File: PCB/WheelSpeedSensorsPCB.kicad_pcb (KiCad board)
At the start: 2 copper layers, 60 x 90 mm, 21 parts, among them J1 RearLeftWheel, J10 FrontRightShock, J11 RearRightShock, J2 FrontRightWheel, J3 RearRightWheel, J4 Conn_01x02_Pin, J5 FrontLeftWheel, J6 RearLeftShock, J7 VehicleBus, J8 Conn_01x02_Pin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

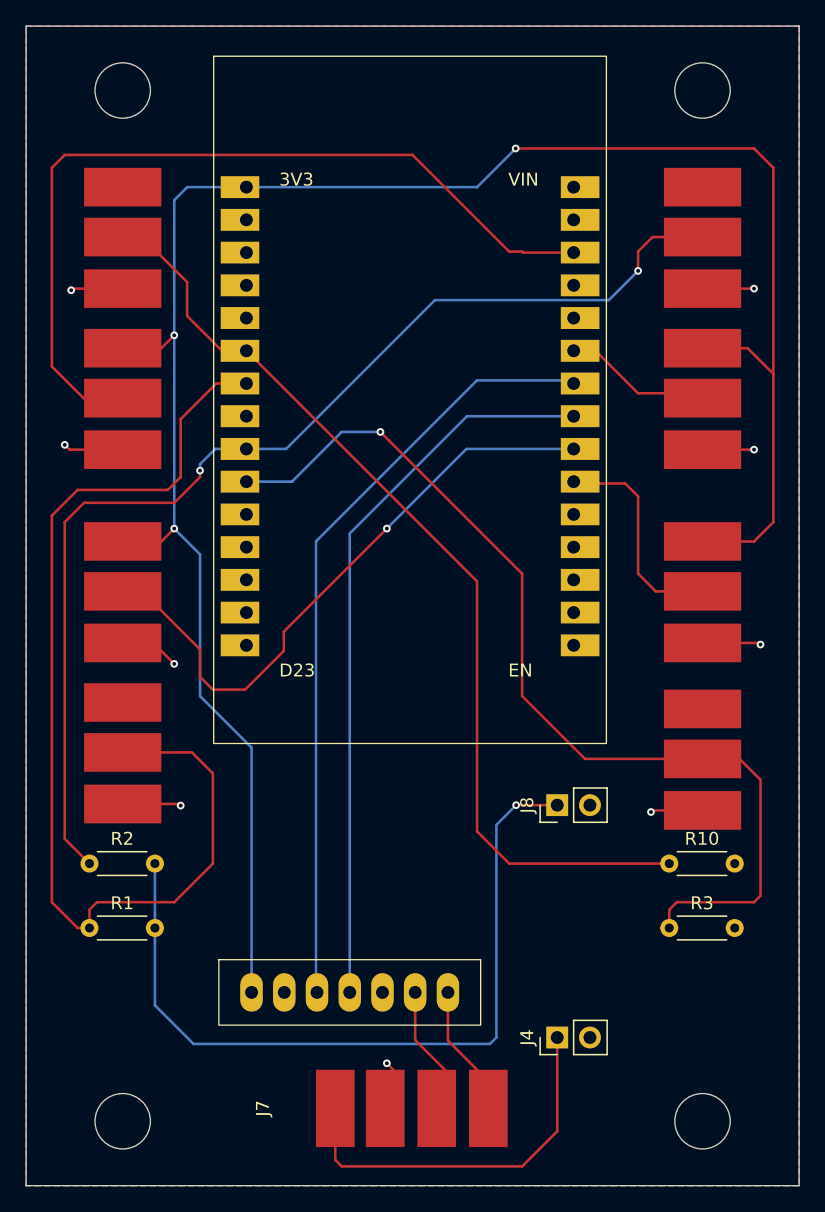
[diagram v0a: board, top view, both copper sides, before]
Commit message: Update PCB and GBRs to have Silkscreen
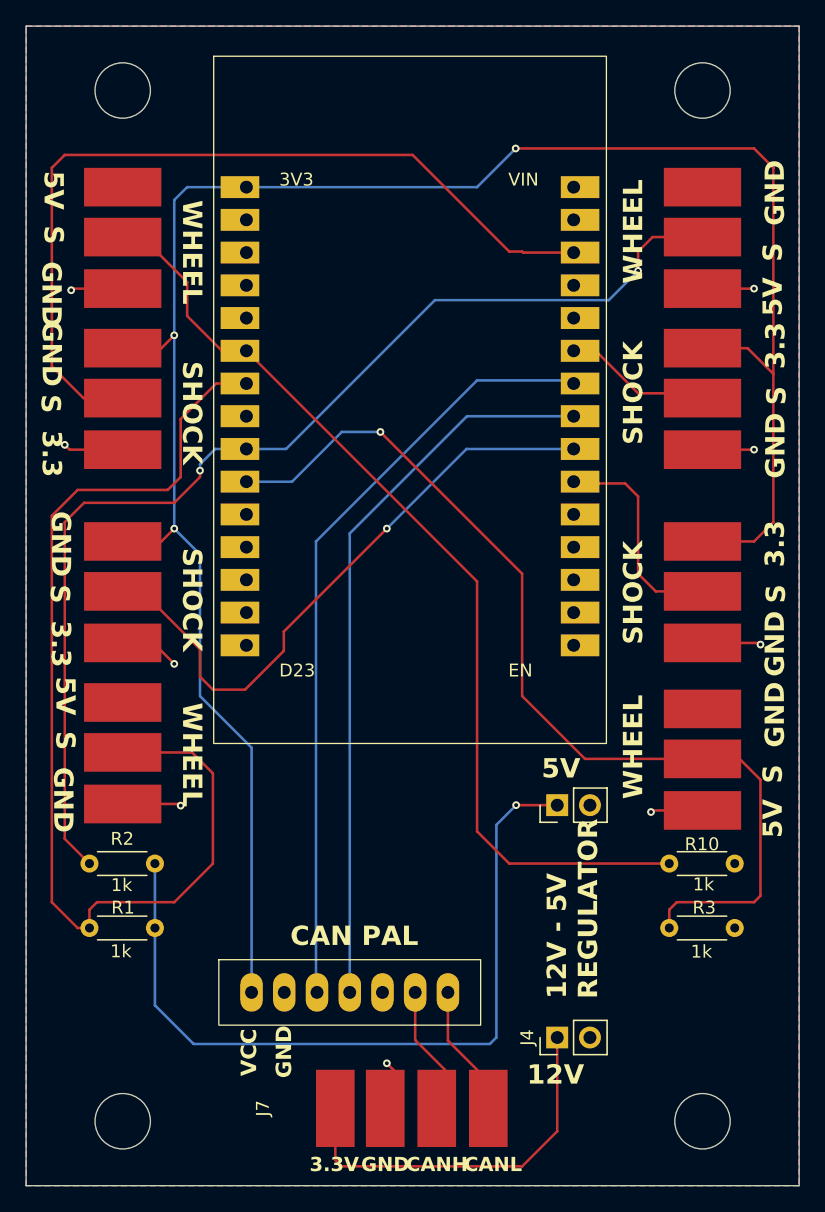
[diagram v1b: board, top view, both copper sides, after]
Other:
- board text added: "12V"
- board text added: "12V - 5V REGULATOR"
- board text added: "1k"
- board text added: "3.3"
- board text added: "3.3V"
- board text added: "5V"
- board text added: "CAN PAL"
- board text added: "CANH"
- board text added: "CANL"
- board text added: "GND"
- board text added: "S"
- board text added: "SHOCK"
- board text added: "VCC"
- board text added: "WHEEL"

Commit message: Fix silkscreen mistake on vehicle bus connection
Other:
- board text removed: "3.3V"
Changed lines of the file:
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@@
 		)
 	)
-	(gr_text "3.3V"
-		(at 127 141.5 0)
+	(gr_text "12V"
+		(at 127.200726 141.490471 0)
 		(layer "F.SilkS")
 		(effects
